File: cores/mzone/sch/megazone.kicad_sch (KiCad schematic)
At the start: 25 parts

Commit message: mzone core
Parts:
- renumbered A_B14 to B_B14, A_C13 to B_C13, A_D15 to B_D15, A_DE11 to B_DE11, A_DE12 to B_DE12, A_DE13 to B_DE13, A_DE9 to B_DE9, A_F14 to B_F14, A_G14 to B_G14

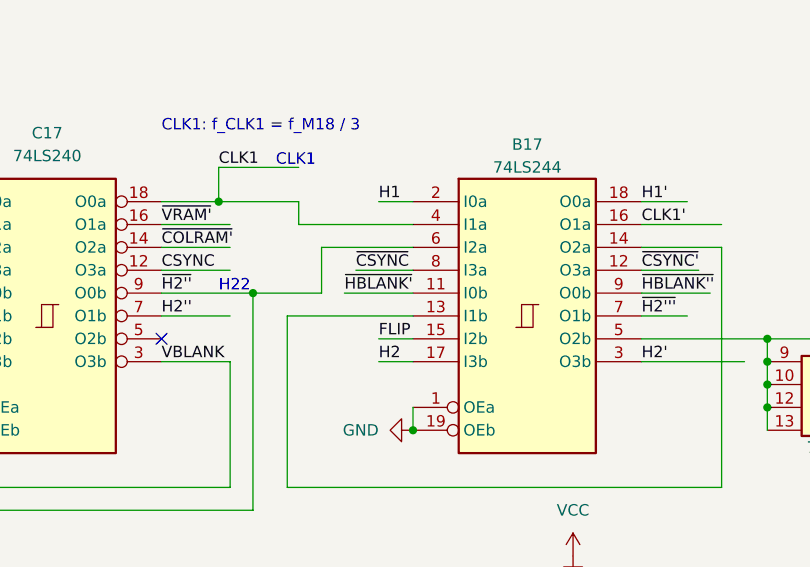
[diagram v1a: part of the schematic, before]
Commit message: mzone core
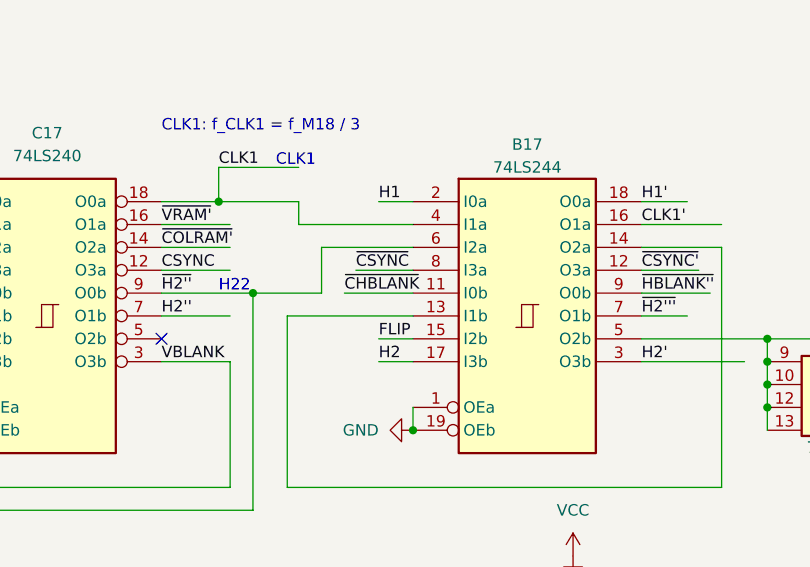
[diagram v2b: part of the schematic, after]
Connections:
- net ~{HBLANK'} renamed ~{CHBLANK}
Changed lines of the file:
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@@
 		)
 	)
-	(label "~{HBLANK'}"
+	(label "~{CHBLANK}"
 		(at 187.96 87.63 0)
 		(fields_autoplaced yes)
